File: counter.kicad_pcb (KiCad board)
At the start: 2 copper layers, 60 x 100 mm, 39 parts, among them J1 Eurorack Power, J2 Clock In 1, J3 Reset In 1, J4 Clock In 2, J5 Reset In 2, Q1 2N3904, Q2 2N3904, SW1 Reset 1, SW2 Reset 2, U1 LM7805_TO220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

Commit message: Add panel
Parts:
- added REF**: Untitled, MAI_Logo:MAI_Logo_10mm_Silkscreen, F.Cu at (86.7, 117.2)
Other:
- board text added: "Counter rev. 1 Sept 27, 2025"

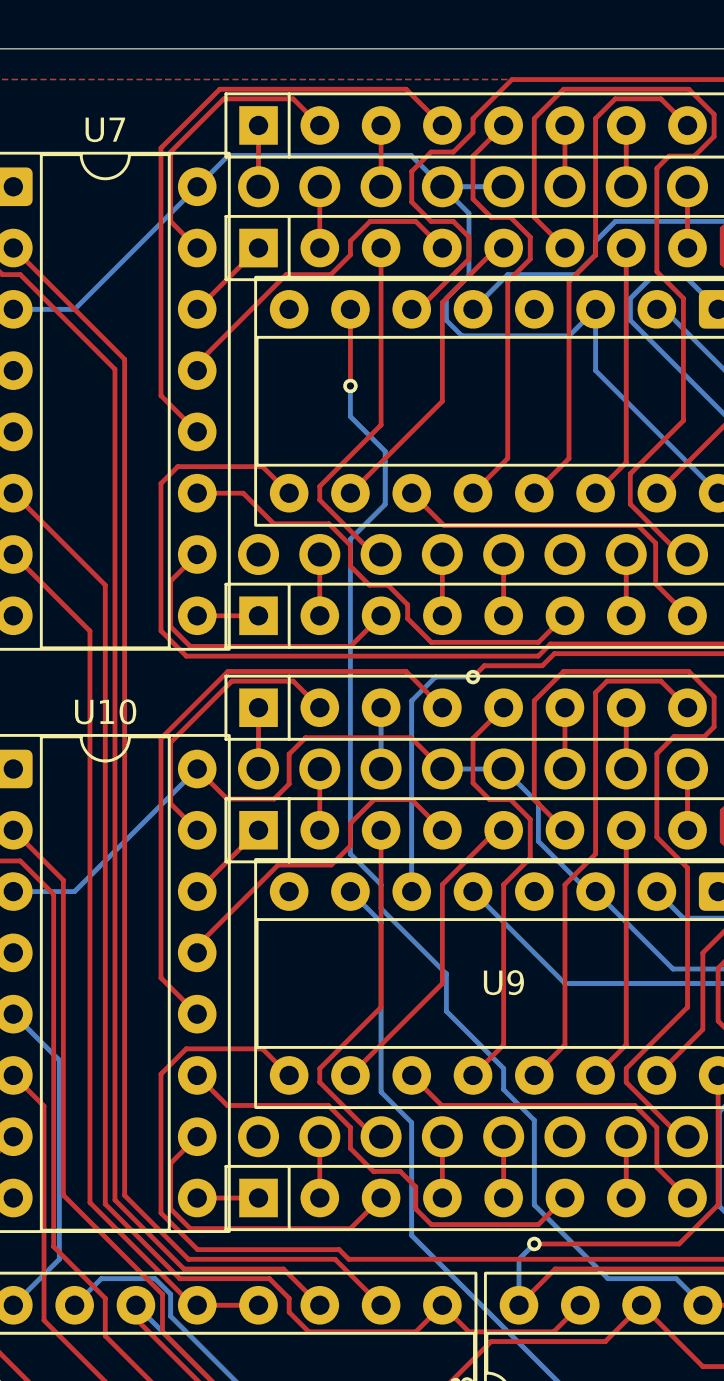
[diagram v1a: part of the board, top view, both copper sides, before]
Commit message: Fix ones place digit being backwards
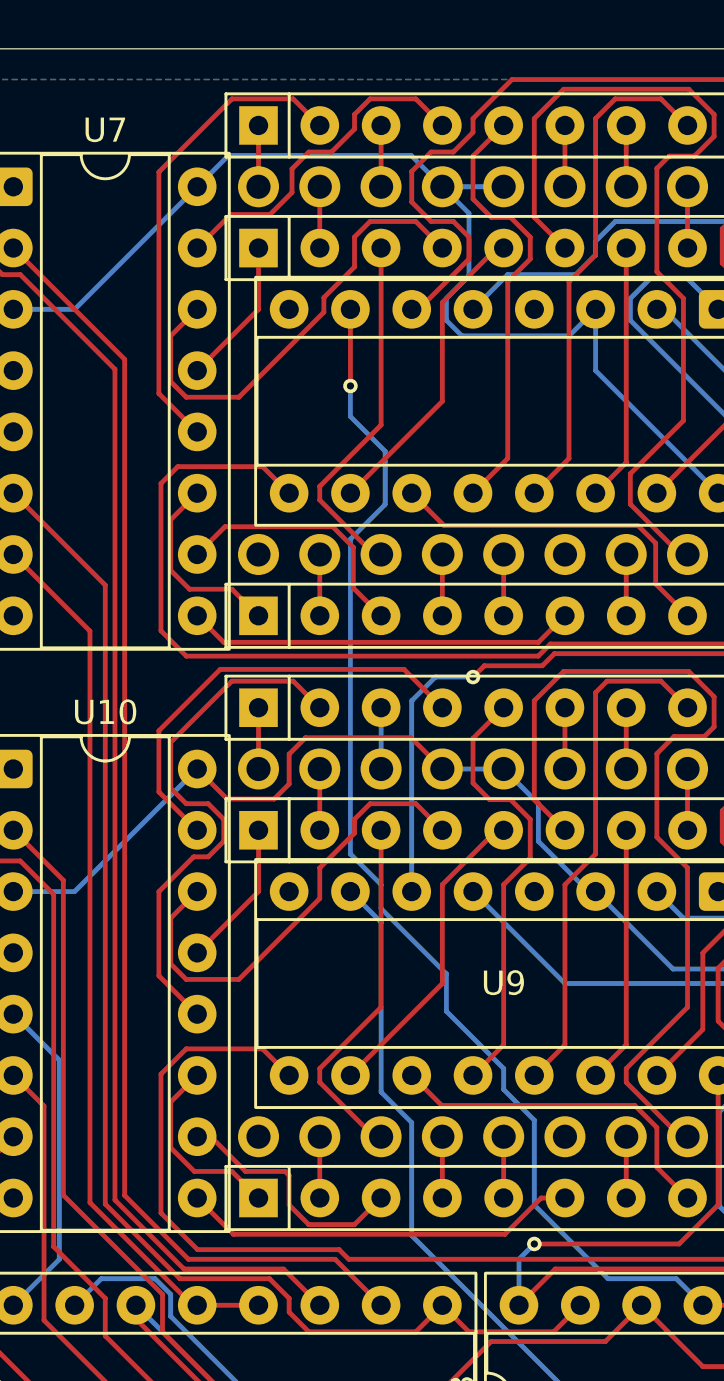
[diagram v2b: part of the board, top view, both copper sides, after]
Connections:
- U10 pad 11: Net-(RN6C-R3.2) -> Net-(RN6A-R1.1)
- U10 pad 12: Net-(RN4B-R2.2) -> Net-(RN4A-R1.2)
- U10 pad 13: Net-(RN5B-R2.2) -> Net-(RN5A-R1.1)
- U10 pad 14: Net-(RN5A-R1.1) -> Net-(RN5B-R2.2)
- U10 pad 15: Net-(RN4A-R1.2) -> Net-(RN4B-R2.2)
- U10 pad 9: Net-(RN6A-R1.1) -> Net-(RN6C-R3.2)
- U7 pad 11: Net-(RN3C-R3.2) -> Net-(RN3A-R1.1)
- U7 pad 12: Net-(RN1B-R2.2) -> Net-(RN1A-R1.2)
- U7 pad 13: Net-(RN2B-R2.2) -> Net-(RN2A-R1.1)
- U7 pad 14: Net-(RN2A-R1.1) -> Net-(RN2B-R2.2)
- U7 pad 15: Net-(RN1A-R1.2) -> Net-(RN1B-R2.2)
- U7 pad 9: Net-(RN3A-R1.1) -> Net-(RN3C-R3.2)
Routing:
- net Net-(RN1B-R2.2): track 25.7 -> 14.1 mm
- net Net-(RN4A-R1.2): track 11.8 -> 22.5 mm
- net Net-(RN1A-R1.2): track 12.0 -> 19.8 mm
- net Net-(RN4B-R2.2): track 25.5 -> 18.2 mm
- net Net-(RN2B-R2.2): track 13.7 -> 19.5 mm
- net Net-(RN3A-R1.1): track 2.54 -> 8.07 mm
- net Net-(RN5B-R2.2): track 14.0 -> 19.5 mm
- net Net-(RN6A-R1.1): track 2.54 -> 7.96 mm
- net Net-(RN3C-R3.2): track 19.1 -> 16.2 mm
- net Net-(RN6C-R3.2): track 19.3 -> 16.5 mm
- net Net-(RN6B-R2.1): track 13.0 -> 10.3 mm
- net Net-(RN5A-R1.1): track 3.59 -> 6.13 mm
- net Net-(RN2A-R1.1): track 3.59 -> 6.13 mm
- net Net-(RN3B-R2.1): track 13.0 -> 10.6 mm

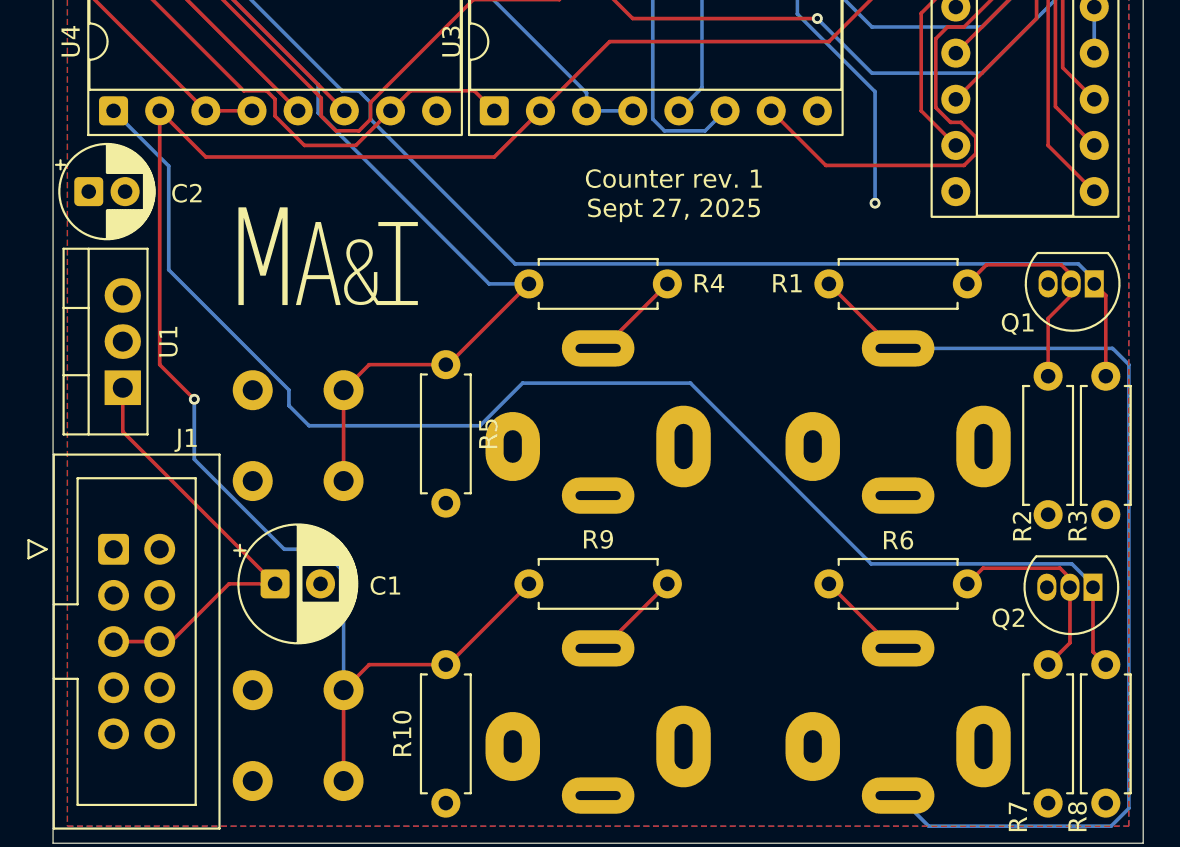
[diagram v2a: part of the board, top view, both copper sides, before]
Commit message: Add diodes to reduce regulator input voltage
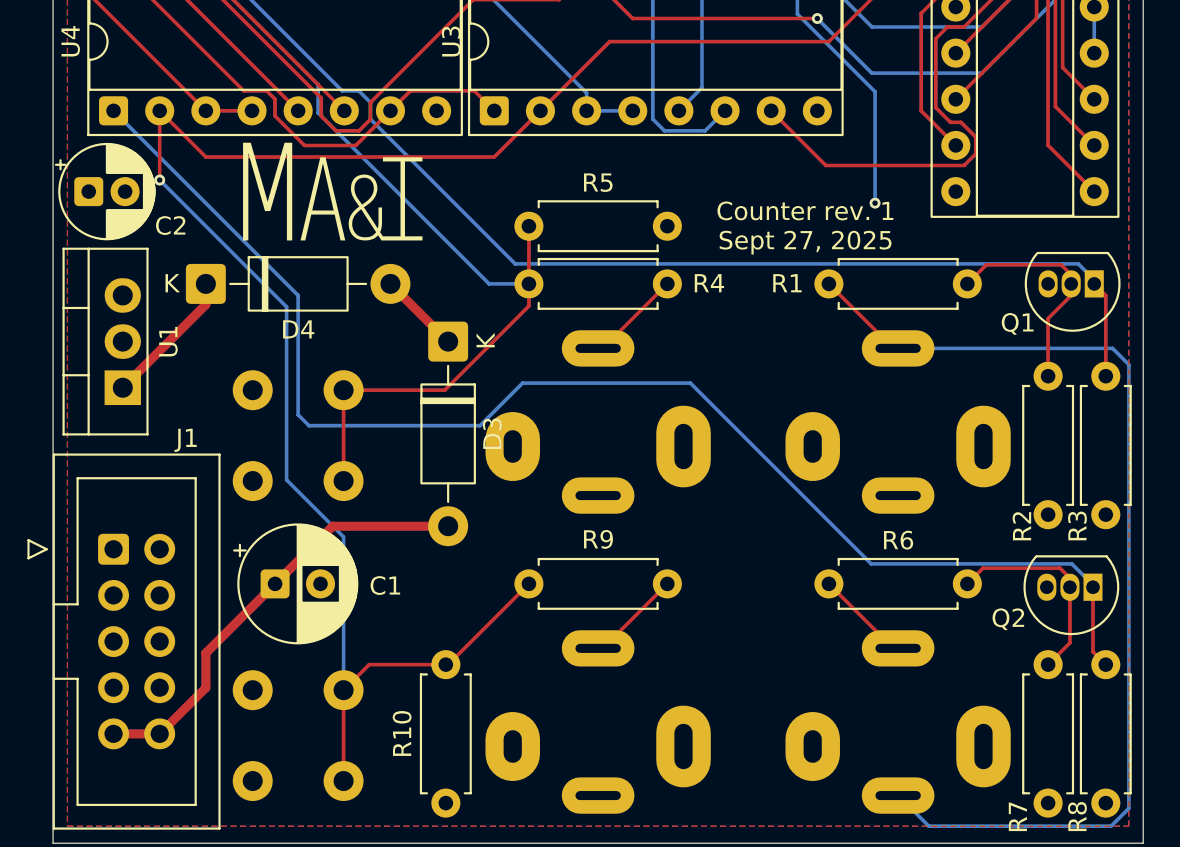
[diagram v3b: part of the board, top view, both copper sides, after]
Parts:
- added D3: 1N4001, Diode_THT:D_DO-41_SOD81_P10.16mm_Horizontal, F.Cu at (93.3, 121.9)
- added D4: 1N4001, Diode_THT:D_DO-41_SOD81_P10.16mm_Horizontal, F.Cu at (80.0, 118.7)
- moved R5 8.89 mm to (97.8, 115.6), turned to 0 degrees
- moved REF** 3.57 mm to (87.0, 113.7)
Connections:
- C1 pad 1: Net-(J1-Pin_5) -> Net-(D3-A)
- J1 pad 10: unconnected-(J1-Pin_10-Pad10) -> Net-(D3-A)
- J1 pad 2: GND -> unconnected-(J1-Pin_2-Pad2)
- J1 pad 5: Net-(J1-Pin_5) -> GND
- J1 pad 6: Net-(J1-Pin_5) -> GND
- J1 pad 9: GND -> Net-(D3-A)
- U1 pad 1: Net-(J1-Pin_5) -> Net-(D4-K)
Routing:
- net Net-(J1-Pin_5): track 24.5 -> 0.00 mm
- net Net-(D3-A): track 0.00 -> 24.3 mm
- net Net-(D4-K): track 0.00 -> 7.61 mm
- net Net-(D3-K): track 0.00 -> 4.49 mm
- net RST1: track 105.8 -> 109.7 mm
- net RST2: track 105.3 -> 104.1 mm
- net GND: track 14.9 -> 15.5 mm
